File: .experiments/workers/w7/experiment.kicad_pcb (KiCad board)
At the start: 2 copper layers, 140 x 90 mm, 39 parts, among them J1 USB_C, J2 Output, J3 Debug, Q1 FS8205A, U1 USBLC6-2SC6, U2 BQ24072, U3 HY2113-KB5B, U4 MT3608, U5 AP2112K-3.3, U6 LN61CN3302MR-G

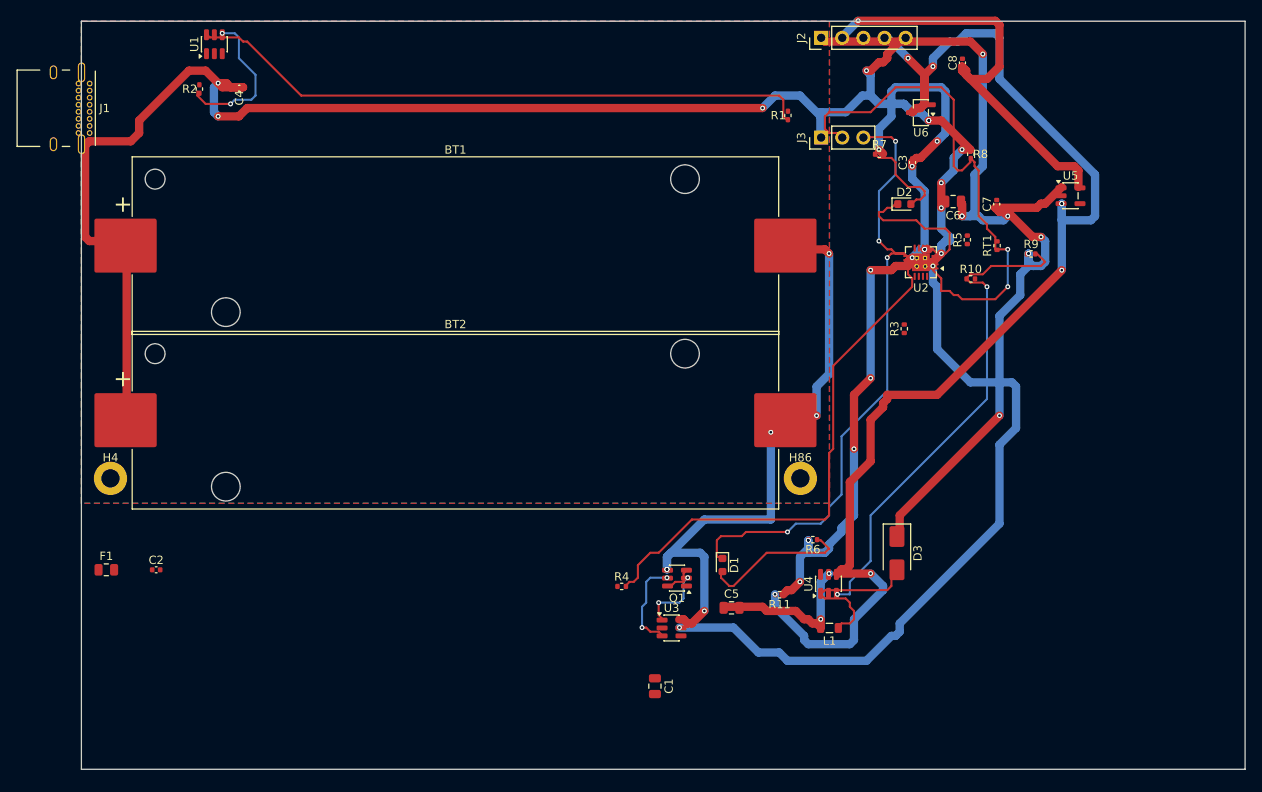
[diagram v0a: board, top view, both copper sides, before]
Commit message: 35-round experiment: best score 25.33, improved routing params
Router and conflict resolution tuning from autonomous optimization loop.
Best config: clearance=0.2051mm, cooling_factor=0.9735, existing_trace_cost=200.0

Co-Authored-By: Claude Opus 4.6 <noreply@anthropic.com>
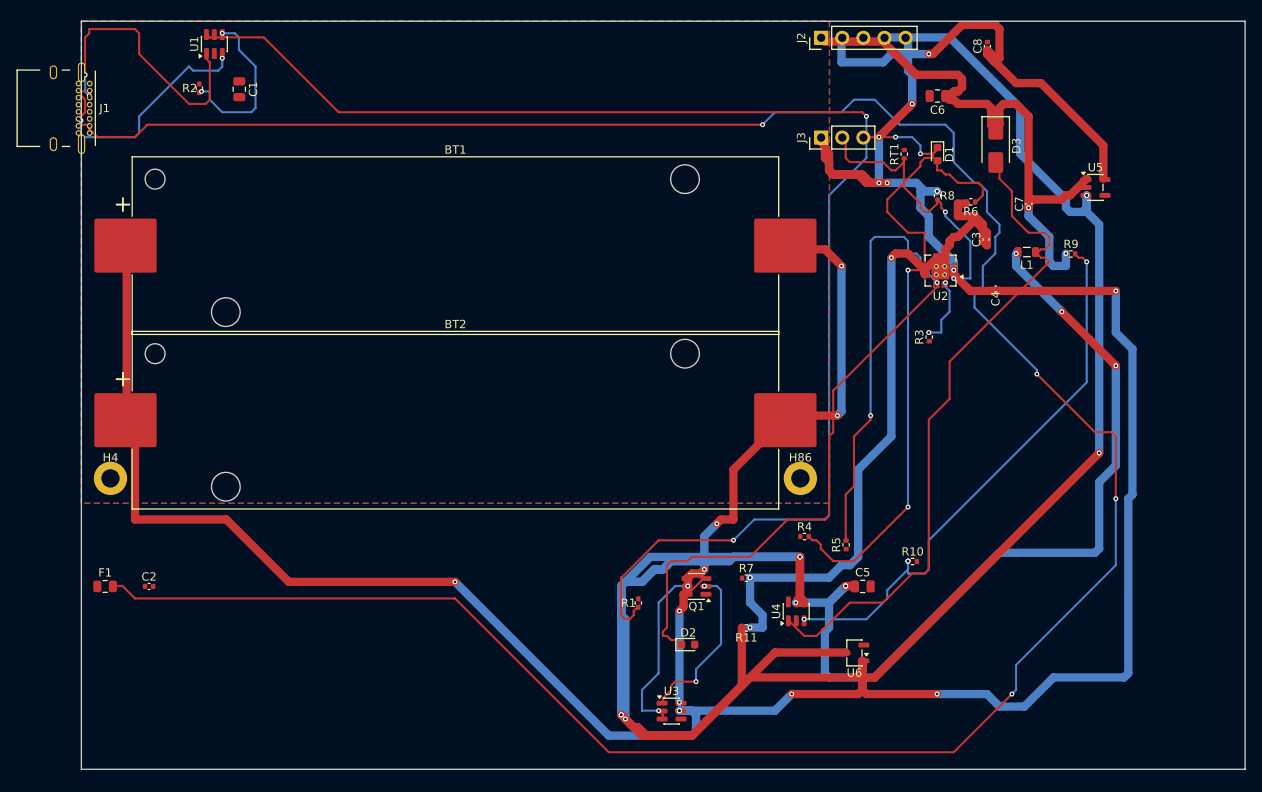
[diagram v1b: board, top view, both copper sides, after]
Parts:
- moved C4 94.2 mm to (110.0, 32.2)
- moved C1 87.5 mm to (19.0, 8.19)
- moved U6 65.5 mm to (93.0, 76.0)
- moved R1 61.4 mm to (67.0, 70.0)
- moved D2 59.0 mm to (73.0, 75.0)
- moved D1 55.8 mm to (103.0, 16.0)
- moved R7 53.5 mm to (80.0, 67.0)
- moved L1 51.1 mm to (113.7, 27.8)
- moved D3 50.4 mm to (110.0, 15.0)
- moved R6 44.9 mm to (107.0, 21.7)
- moved R5 39.5 mm to (92.0, 63.0)
- moved R10 34.7 mm to (100.0, 65.0)
- moved R4 22.8 mm to (87.0, 62.0)
- moved C5 16.0 mm to (94.0, 68.0)
- moved RT1 15.7 mm to (99.0, 16.0)
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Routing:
- net Net-(F1-Pad2): track 0.00 -> 319.0 mm, vias 0 -> 4
- net /EN: track 149.0 -> 332.9 mm, vias 8 -> 10
- net Net-(R1-Pad1): track 75.5 -> 169.2 mm, vias 0 -> 2
- net /VSYS_BOOST: track 19.4 -> 101.3 mm, vias 2 -> 6
- net Net-(D3-A): track 19.7 -> 81.8 mm
- net Net-(D2-K): track 18.7 -> 70.0 mm
- net Net-(U2-TMR): track 0.00 -> 49.2 mm, vias 0 -> 2
- net /5V: track 115.5 -> 69.3 mm, vias 8 -> 2
- net /CHG_N: track 75.4 -> 30.7 mm, vias 4 -> 2
- net Net-(J1-CC1): track 0.00 -> 34.0 mm, vias 0 -> 2
- net /NTC_SENSE: track 62.8 -> 34.3 mm
- net Net-(J1-CC2): track 0.00 -> 25.6 mm, vias 0 -> 2
- net /VBAT: track 293.0 -> 310.7 mm
- net Net-(U2-ILIM): track 62.7 -> 47.4 mm, vias 0 -> 2
- net Net-(Q1A-G): track 8.12 -> 20.1 mm
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
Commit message: 45-round experiment: best score 25.66, all nets routed (26/26)
Fixed A* performance by increasing max_search from 100k->500k to handle
high trace costs (100.0) without timing out. Kept high cost + coarse grid
(0.5mm) to prevent shorts while still routing efficiently.

Best config: edge_margin=5.7493mm, cooling_factor=0.9764, existing_trace_cost=200, max_rips=8

Co-Authored-By: Claude Opus 4.6 <noreply@anthropic.com>
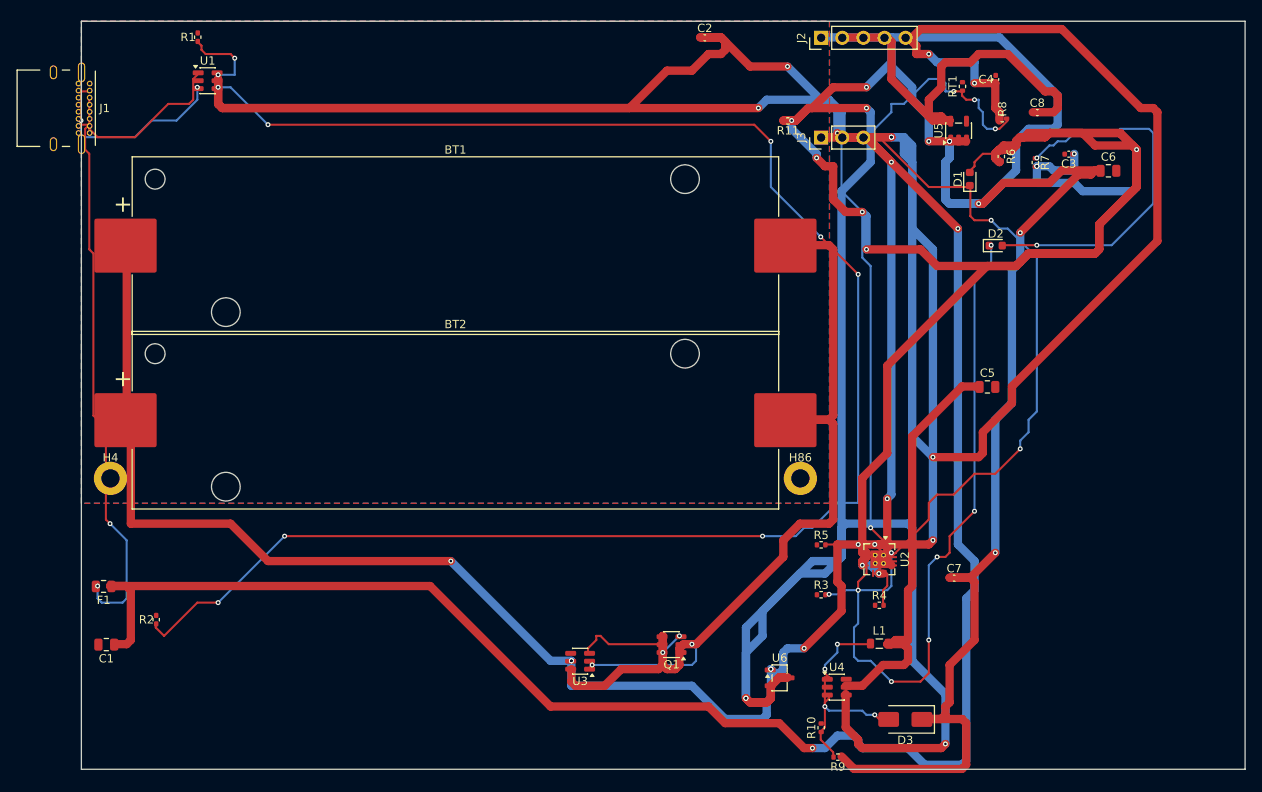
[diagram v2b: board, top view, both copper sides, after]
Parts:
- moved C2 93.9 mm to (75.0, 2.00)
- moved R1 86.3 mm to (14.0, 1.92)
- moved D3 69.9 mm to (99.1, 84.0), turned to 180 degrees
- moved C1 68.7 mm to (3.00, 75.0), turned to 180 degrees
- moved R9 66.7 mm to (91.0, 88.5), turned to 180 degrees
- moved R2 64.1 mm to (9.00, 72.0)
- moved R11 61.2 mm to (85.0, 12.0)
- moved R7 60.9 mm to (114.8, 17.0), turned to -90 degrees
- moved D2 60.6 mm to (110.0, 27.0)
- moved L1 50.3 mm to (96.0, 74.9), turned to 0 degrees
- moved C7 45.9 mm to (105.0, 67.0), turned to 0 degrees
- moved U2 35.5 mm to (96.0, 64.7), turned to -90 degrees
- moved R3 33.6 mm to (89.0, 69.0), turned to 0 degrees
- moved C5 28.3 mm to (109.0, 44.0)
- moved C4 25.2 mm to (110.0, 7.00), turned to 90 degrees
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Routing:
- net /VBUS: track 0.00 -> 441.8 mm, vias 0 -> 8
- net Net-(F1-Pad2): track 319.0 -> 70.7 mm, vias 4 -> 2
- net Net-(R2-Pad1): track 20.4 -> 209.1 mm, vias 2 -> 8
- net Net-(R1-Pad1): track 169.2 -> 9.62 mm
- net /VSYS: track 87.7 -> 225.5 mm, vias 4 -> 10
- net /5V: track 69.3 -> 198.9 mm, vias 2 -> 6
- net /EN: track 332.9 -> 225.1 mm, vias 10 -> 8
- net /VBAT: track 310.7 -> 381.9 mm, vias 14 -> 12
- net Net-(D3-A): track 81.8 -> 20.9 mm, vias 0 -> 4
- net Net-(U4-FB): track 67.6 -> 8.54 mm, vias 4 -> 0
- net /VSYS_BOOST: track 101.3 -> 50.8 mm, vias 6 -> 0
- net /CHG_N: track 30.7 -> 77.8 mm
- net /NTC_SENSE: track 34.3 -> 80.0 mm, vias 2 -> 6
- net Net-(D2-A): track 0.00 -> 44.2 mm, vias 0 -> 2
- net Net-(U2-ILIM): track 47.4 -> 4.21 mm, vias 2 -> 0
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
